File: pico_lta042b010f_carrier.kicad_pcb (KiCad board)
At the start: 2 copper layers, 120 x 70 mm, 31 parts, among them J1 LTA042B010F_FFC_36P_0.5mm, J2 5V_INPUT, J3 CCFL_INVERTER_13V8, U1 RaspberryPi_Pico_2W, U3 MC34063AD

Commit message: chore(kicad): checkpoint before PCB artwork
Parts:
- C11: value 10u 25V (+ to GND) -> 10uF 50V (+ to GND)
- C6: value 220u 16V -> 220uF 35V; footprint Capacitor_THT:CP_Radial_D5.0mm_P2.00mm -> Capacitor_THT:CP_Radial_D8.0mm_P3.50mm
- C7: value 470p -> 470pF 50V C0G; footprint Capacitor_SMD:C_0805_2012Metric -> Capacitor_THT:C_Disc_D5.0mm_W2.5mm_P2.50mm
- C8: value 47u 25V -> 47uF 35V
- C9: value 10u 25V -> 10uF 50V
- D4, D6, D7: footprint Diode_SMD:D_SMA -> Diode_THT:D_DO-41_SOD81_P10.16mm_Horizontal
- L1: value 150uH -> 100uH; footprint Inductor_SMD:L_Sunlord_MWSA1204S-150 -> Inductor_SMD:L_Taiyo-Yuden_NR-10050_9.8x10.0mm_HandSoldering
- R7: footprint Resistor_SMD:R_2512_6332Metric_Pad1.40x3.35mm_HandSolder -> Resistor_THT:R_Axial_DIN0207_L6.3mm_D2.5mm_P10.16mm_Horizontal
- R8: footprint Resistor_SMD:R_0805_2012Metric -> Resistor_SMD:R_0603_1608Metric
- moved R7 10.0 mm to (72.0, 12.0)
- moved D4 6.00 mm to (94.0, 22.0)
- moved D7 2.00 mm to (108.0, 22.0)
- moved R8 2.00 mm to (80.0, 35.0)

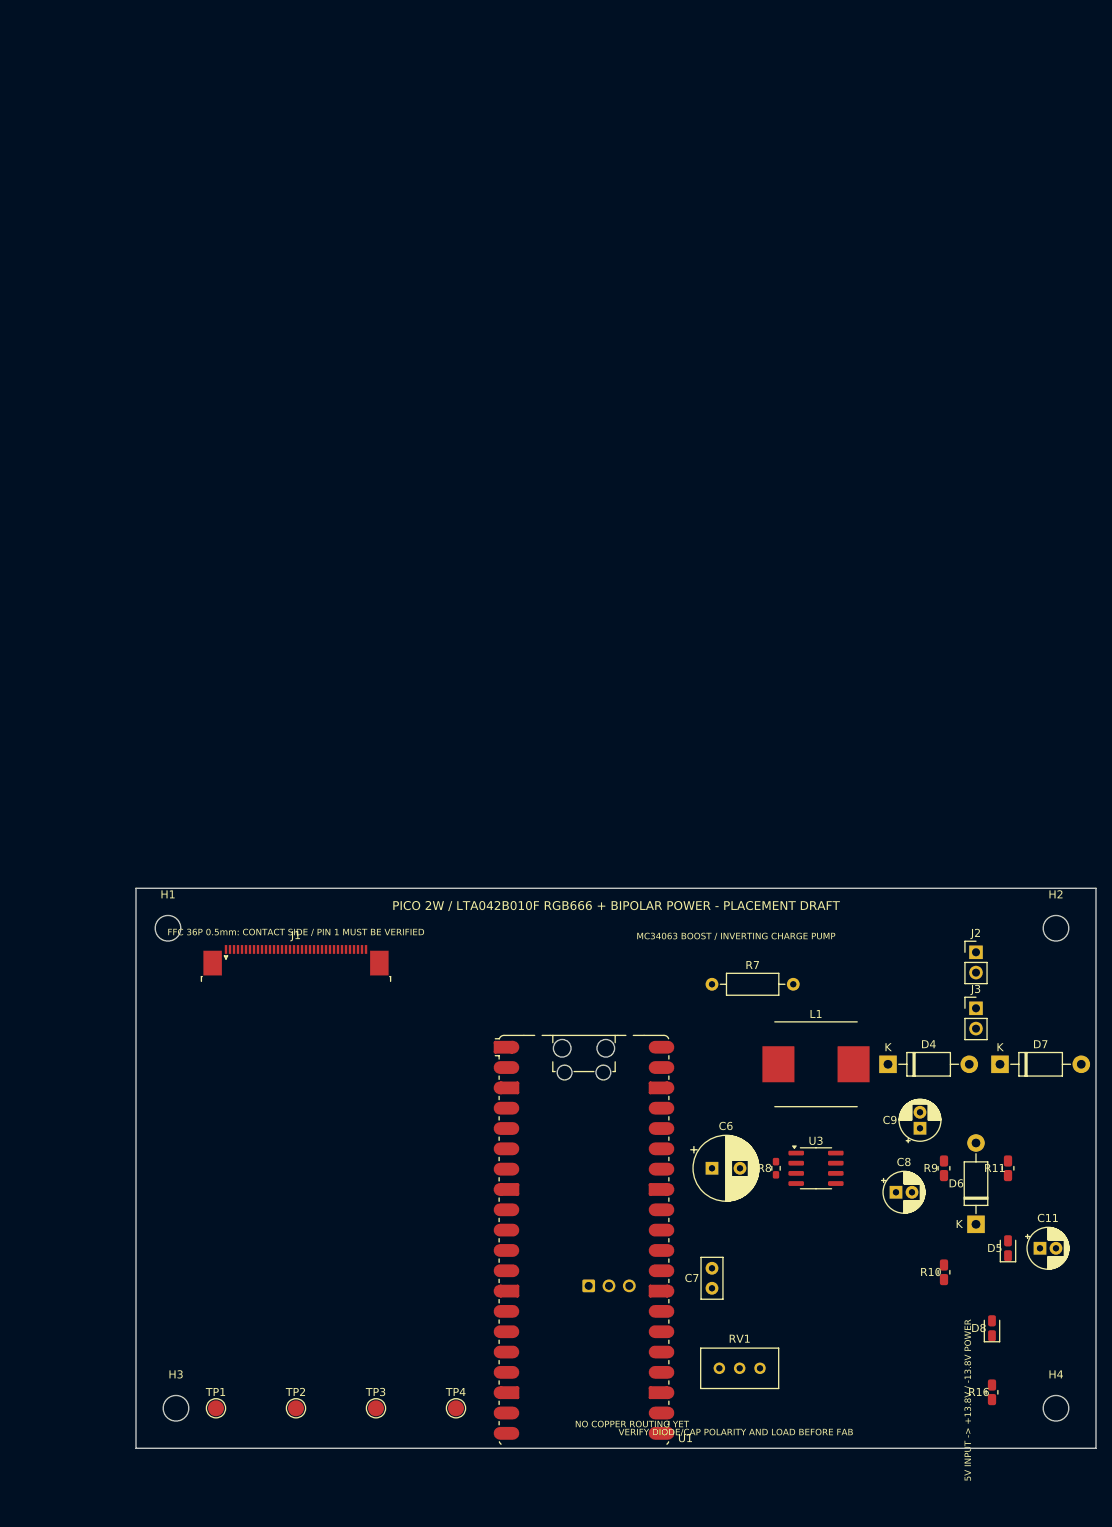
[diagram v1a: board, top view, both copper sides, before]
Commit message: Update hand-solder components and preserve current PCB layout
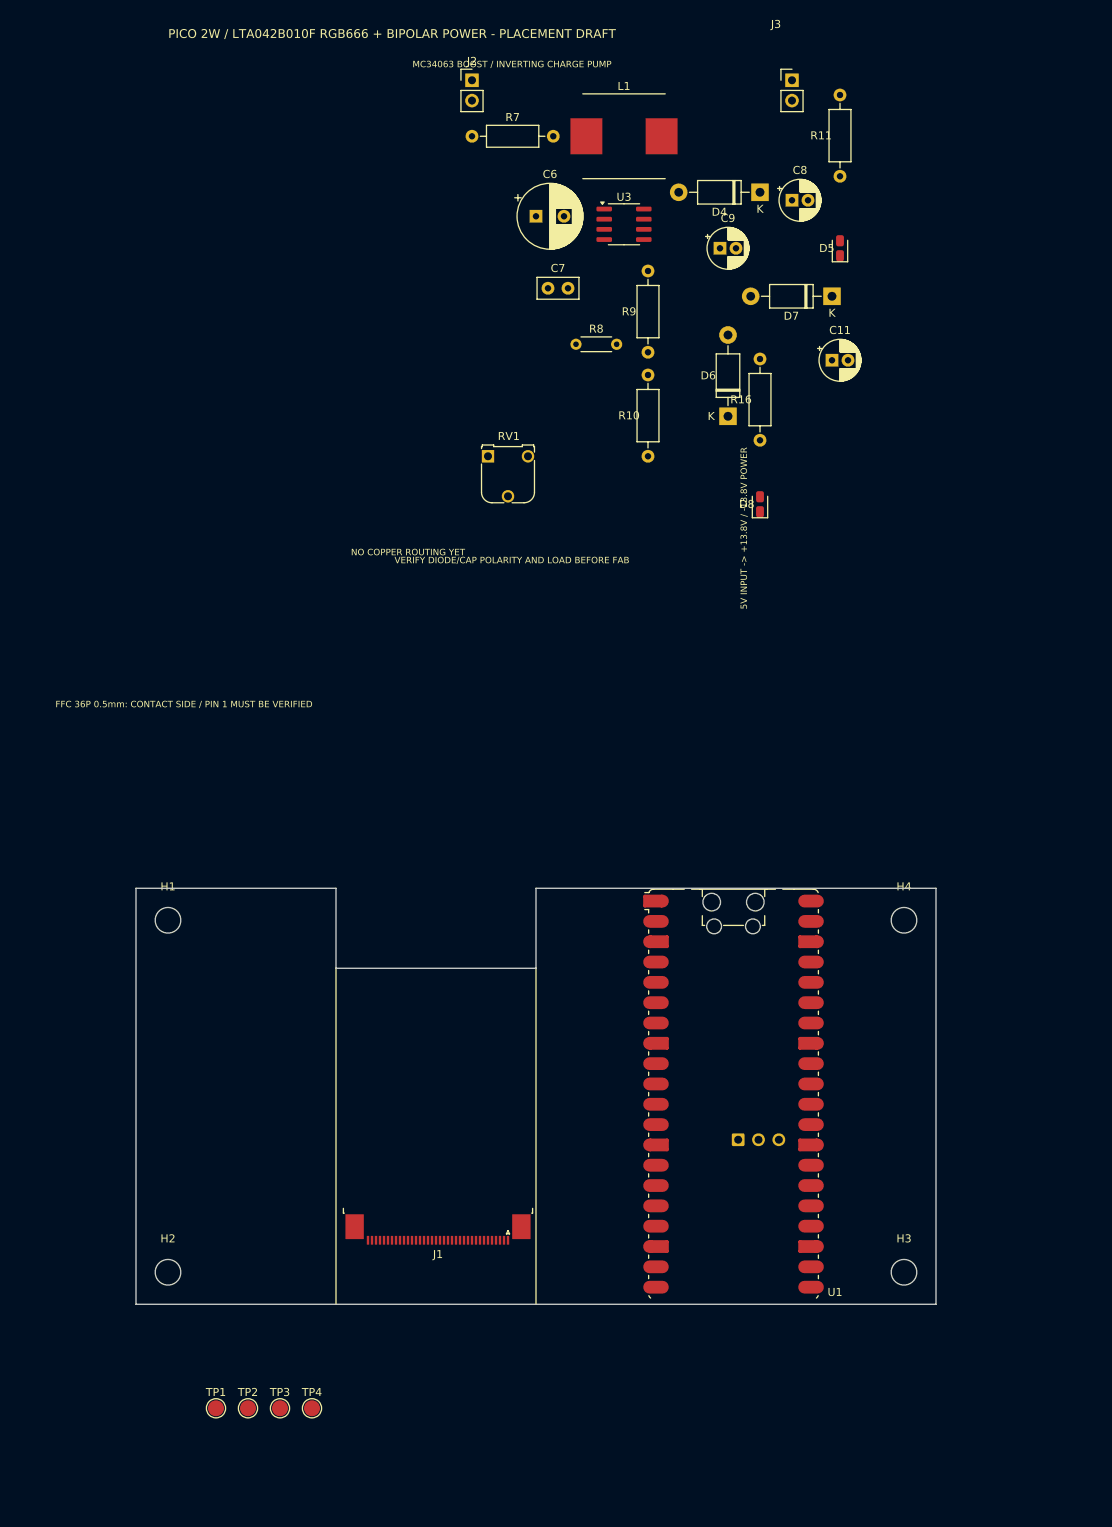
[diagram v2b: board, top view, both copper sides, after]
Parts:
- R10: value 1k -> 1k 0.1%; footprint Resistor_SMD:R_0805_2012Metric -> Resistor_THT:R_Axial_DIN0207_L6.3mm_D2.5mm_P10.16mm_Horizontal
- R11, R16, R9: value 10k -> 10k 0.1%; footprint Resistor_SMD:R_0805_2012Metric -> Resistor_THT:R_Axial_DIN0207_L6.3mm_D2.5mm_P10.16mm_Horizontal
- R8: value 200 -> 200 1%; footprint Resistor_SMD:R_0603_1608Metric -> Resistor_THT:R_Axial_DIN0204_L3.6mm_D1.6mm_P5.08mm_Horizontal
- RV1: footprint Potentiometer_THT:Potentiometer_Bourns_3296W_Vertical -> Potentiometer_THT:Potentiometer_Runtron_RM-065_Vertical
- moved D5 126.8 mm to (88.0, -80.0)
- moved C7 126.7 mm to (51.5, -75.0), turned to 0 degrees
- moved J2 125.9 mm to (42.0, -101.0)
- moved R11 125.8 mm to (88.0, -89.0)
- moved C8 124.7 mm to (82.0, -86.0)
- moved R16 122.5 mm to (78.0, -56.0)
- moved C6 121.0 mm to (50.0, -84.0)
- moved U3 120.4 mm to (61.0, -83.0)
- moved H2 119.0 mm to (4.00, 48.0)
- moved RV1 119.0 mm to (44.0, -54.0)
- moved L1 118.5 mm to (61.0, -94.0)
- moved J3 118.3 mm to (82.0, -101.0)
- moved C11 114.0 mm to (87.0, -66.0)
- moved C9 112.8 mm to (73.0, -80.0), turned to 0 degrees
- moved D4 110.2 mm to (78.0, -87.0), turned to 180 degrees
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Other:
- board size 120 x 70 mm -> 100 x 52 mm

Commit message: Update power-stage layout and component selections
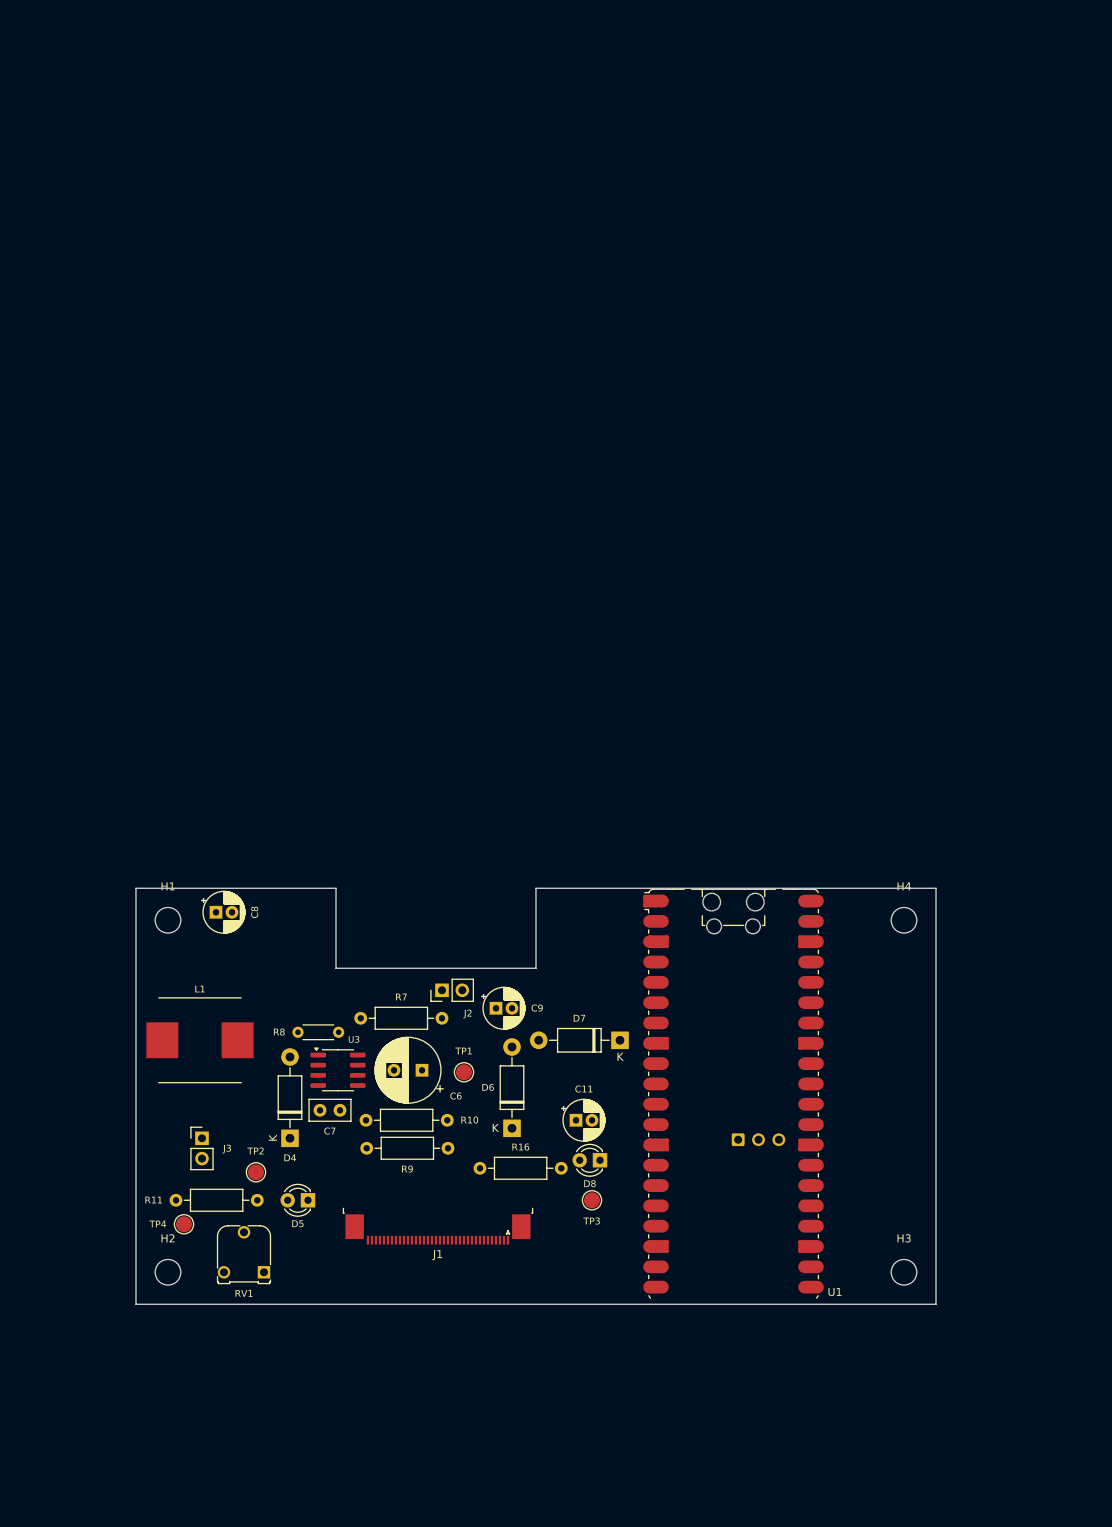
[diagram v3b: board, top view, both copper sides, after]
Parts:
- D5: value GREEN LED -> GREEN LED 3mm; footprint LED_SMD:LED_0805_2012Metric -> LED_THT:LED_D3.0mm
- D8: value RED LED -> RED LED 3mm; footprint LED_SMD:LED_0805_2012Metric -> LED_THT:LED_D3.0mm
- moved R11 152.6 mm to (5.00, 39.0), turned to 0 degrees
- moved J3 151.4 mm to (8.25, 31.2)
- moved D5 136.3 mm to (21.5, 39.0), turned to 180 degrees
- moved D4 132.0 mm to (19.2, 31.2), turned to 90 degrees
- moved L1 124.8 mm to (8.00, 19.0)
- moved C8 114.5 mm to (10.0, 3.00)
- moved J2 113.8 mm to (38.2, 12.8), turned to 90 degrees
- moved U3 111.6 mm to (25.2, 22.8)
- moved R7 110.3 mm to (38.2, 16.2), turned to 180 degrees
- moved C6 107.7 mm to (35.8, 22.8), turned to 180 degrees
- moved C7 106.6 mm to (23.0, 27.8)
- moved RV1 105.8 mm to (16.0, 48.0), turned to 180 degrees
- moved R9 102.6 mm to (39.0, 32.5), turned to 180 degrees
- moved C11 100.2 mm to (55.0, 29.0)
- moved C9 99.0 mm to (45.0, 15.0)
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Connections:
- C9 pad 1: +13V8 -> SW_NODE

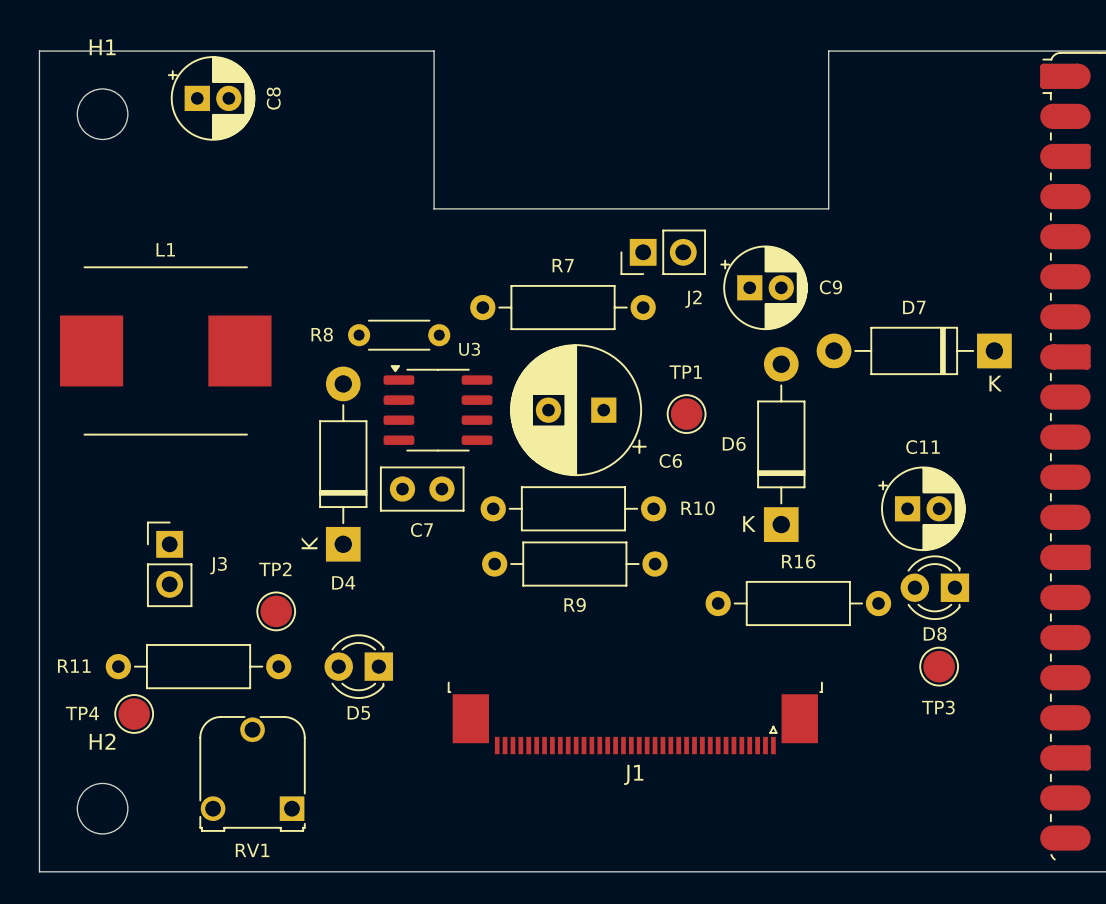
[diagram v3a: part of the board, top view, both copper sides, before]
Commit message: Constrain power components to red placement zone
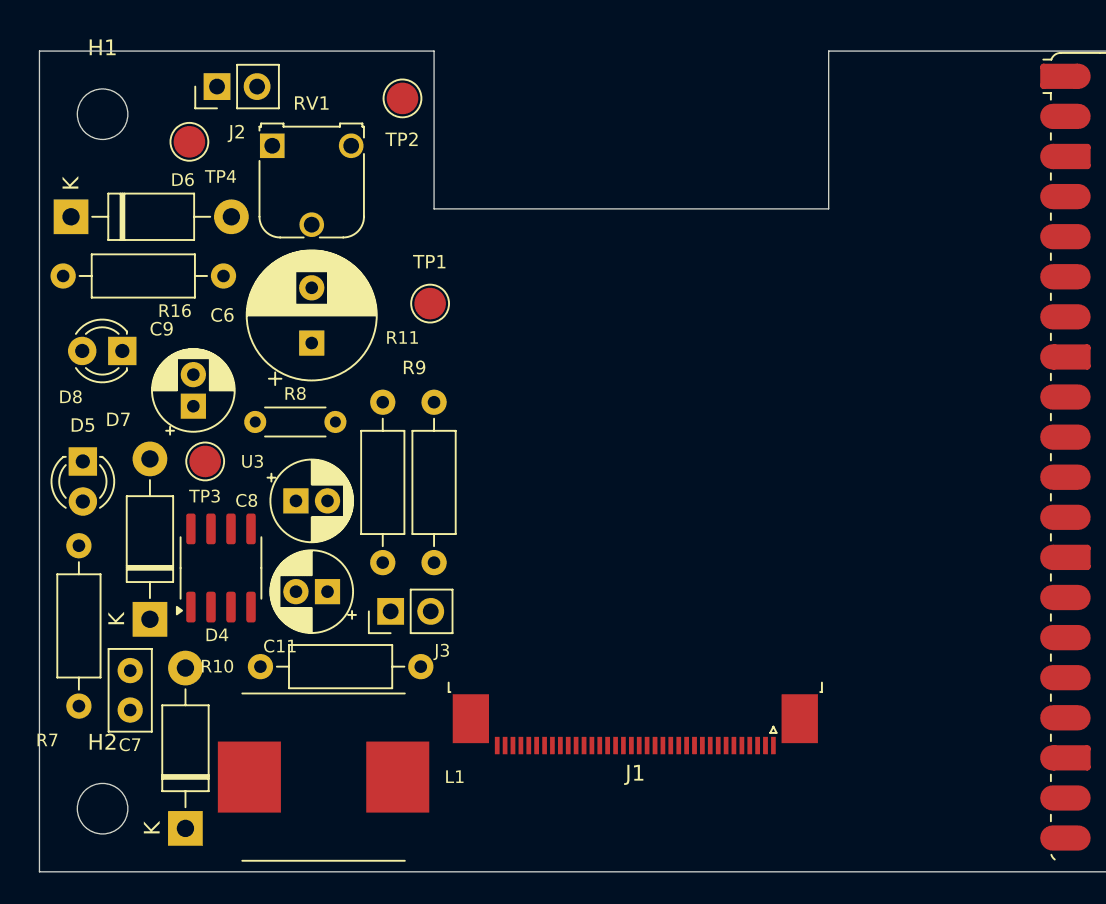
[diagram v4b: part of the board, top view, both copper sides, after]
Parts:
- moved D7 56.1 mm to (7.00, 36.0), turned to 90 degrees
- moved D8 54.8 mm to (5.25, 19.0)
- moved D6 49.0 mm to (2.00, 10.5), turned to 0 degrees
- moved TP3 48.3 mm to (10.5, 26.0), turned to 90 degrees
- moved R16 46.4 mm to (1.50, 14.2)
- moved R7 43.8 mm to (2.50, 41.5), turned to 90 degrees
- moved RV1 42.0 mm to (14.8, 6.00), turned to 0 degrees
- moved C11 37.1 mm to (18.2, 34.2), turned to 180 degrees
- moved TP4 36.4 mm to (9.50, 5.75), turned to 90 degrees
- moved C9 36.0 mm to (9.75, 22.5), turned to 90 degrees
- moved TP2 33.5 mm to (23.0, 3.00), turned to 90 degrees
- moved J2 29.0 mm to (11.2, 2.25)
- moved L1 28.8 mm to (18.0, 46.0), turned to 180 degrees
- moved C8 26.3 mm to (16.2, 28.5)
- moved R11 26.1 mm to (25.0, 22.2), turned to -90 degrees
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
